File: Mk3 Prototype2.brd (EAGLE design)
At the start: 119.6 x 68 mm, 154 parts, among them IC1 TPD3E001DRL, IC2 TPS62082, IC3 STM32F401V, IC4 BQ2409X, IC6 CC3100MOD, IC7 BQ2970, IC8 LSM6DS3, IC9 LIS3MDL, J1 ZX62-AB-5PA(11), J2 ER-TFT024-3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

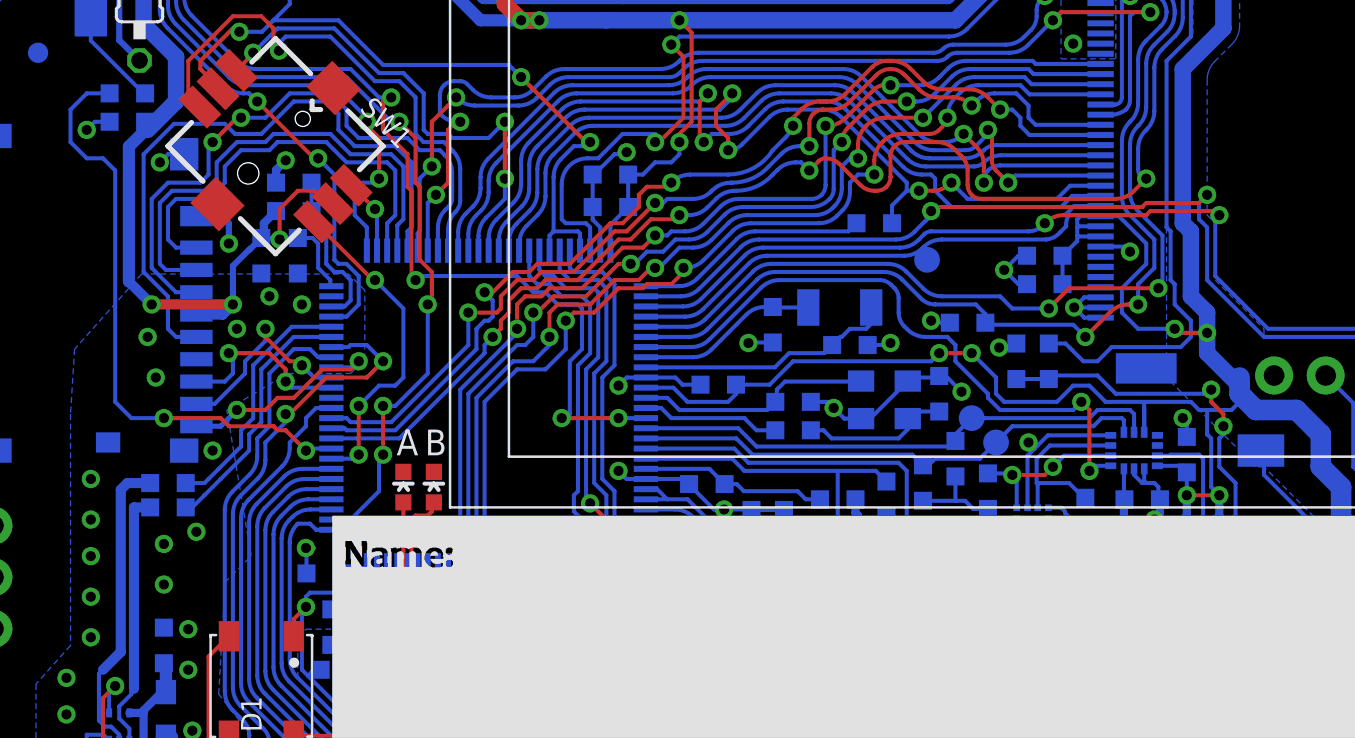
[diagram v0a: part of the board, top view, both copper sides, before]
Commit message: Fix up via clearance
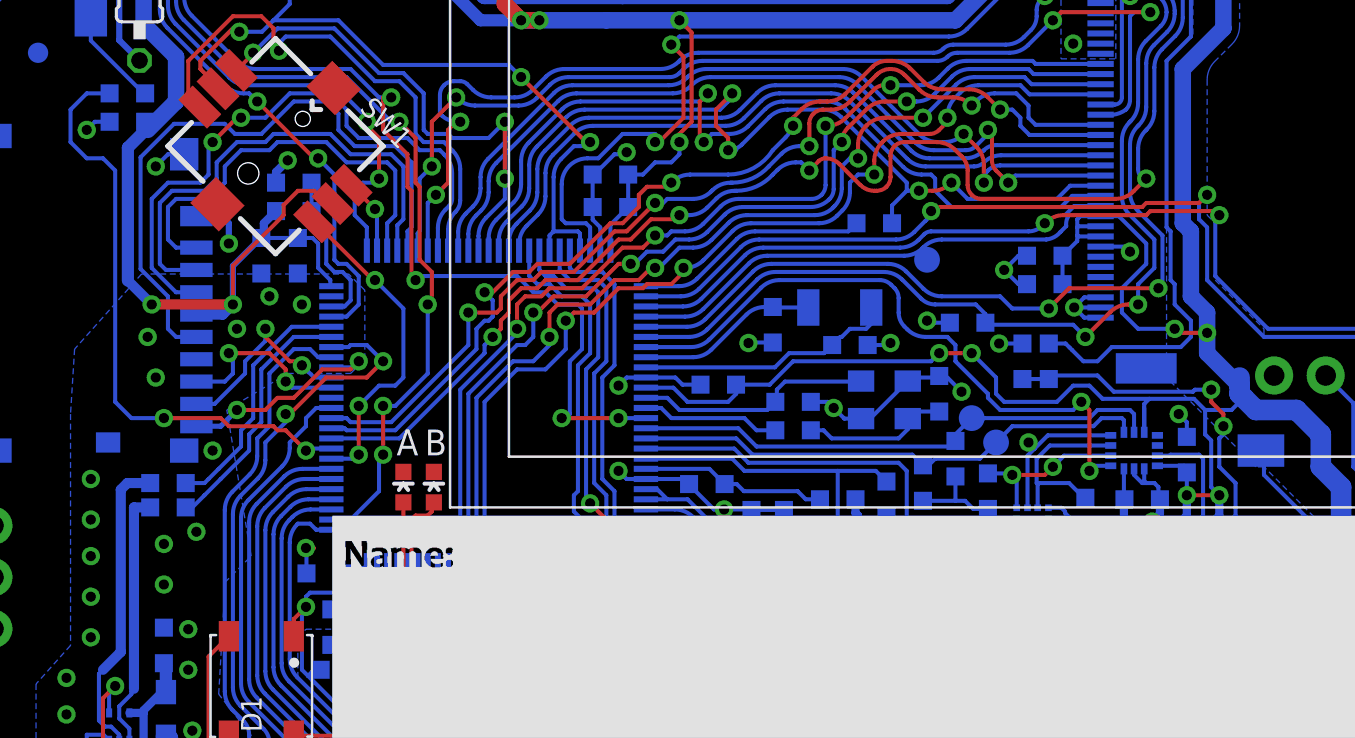
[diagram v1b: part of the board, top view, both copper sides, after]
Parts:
- moved R4 0.30 mm to (58.5, 26.8)
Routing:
- net +3V3: track 526.3 -> 530.2 mm, vias 32 -> 31
- net GND: track 139.9 -> 141.5 mm, vias 155 -> 154

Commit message: minor silk change
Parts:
- moved TP1 2.21 mm to (53.4, 15.8)
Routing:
- net IMU_IRQ1: track 17.0 -> 19.2 mm
- net +3V3: track 530.2 -> 532.3 mm
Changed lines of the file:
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@@
 <element name="LOGO2" library="TiLDA Mk3 Parts" package="UPYTHON_LOGO_SLIKONLY" value="MICROPYTHON-SILK" x="97.2" y="47.9"/>
 <element name="LOGO3" library="TiLDA Mk3 Parts" package="UPYTHON_LOGO_STOPONLY" value="MICROPYTHON-STOP" x="110.9" y="22.9" rot="MR0"/>
-<element name="TP1" library="TiLDA Mk3 Parts" package="B1,27" value="TPB1,27" x="53.6" y="18" smashed="yes" rot="MR0">
-<attribute name="TP_SIGNAL_NAME" value="" x="54.235" y="16.095" size="1" layer="38" rot="MR0"/>
-<attribute name="VALUE" x="54.235" y="17.238" size="0.0254" layer="28" rot="MR0"/>
+<element name="TP1" library="TiLDA Mk3 Parts" package="B1,27" value="TPB1,27" x="53.4" y="15.8" smashed="yes" rot="MR0">
+<attribute name="TP_SIGNAL_NAME" value="" x="54.035" y="13.895" size="1" layer="38" rot="MR0"/>
+<attribute name="VALUE" x="54.035" y="15.038" size="0.0254" layer="28" rot="MR0"/>
 </element>
 </elements>
@@
 <wire x1="56.8" y1="19.525" x2="56.075" y2="19.525" width="0.2" layer="16"/>
 <wire x1="56.8" y1="19.525" x2="56.8" y2="19.2" width="0.2" layer="16"/>
-<wire x1="56.8" y1="19.2" x2="55.2" y2="17.6" width="0.2" layer="16"/>
-<wire x1="55.2" y1="17.6" x2="55.2" y2="16" width="0.2" layer="16"/>
-<wire x1="55.6" y1="15.6" x2="57.125" y2="15.6" width="0.2" layer="16"/>
+<wire x1="55.2" y1="17.6" x2="55.2" y2="15.7" width="0.2" layer="16"/>
+<wire x1="55.2" y1="15.6" x2="57.125" y2="15.6" width="0.2" layer="16"/>
 <wire x1="57.125" y1="15.6" x2="58" y2="16.475" width="0.2" layer="16"/>
 <wire x1="55.675" y1="19.925" x2="56.075" y2="19.525" width="0.2" layer="16"/>
@@
 <wire x1="50.4" y1="19.2" x2="50.4" y2="17.9" width="0.4064" layer="16"/>
 <wire x1="50.4" y1="17.9" x2="50.6" y2="17.7" width="0.4064" layer="16"/>
-<wire x1="50.4" y1="17.9" x2="50.4" y2="16.8" width="0.4064" layer="16"/>
-<wire x1="50.4" y1="16.8" x2="51.2" y2="16" width="0.4064" layer="16"/>
-<wire x1="51.2" y1="16" x2="55.2" y2="16" width="0.4064" layer="16"/>
-<wire x1="55.2" y1="16" x2="55.6" y2="15.6" width="0.4064" layer="16"/>
 <wire x1="62.45" y1="24.95" x2="64.75" y2="24.95" width="0.2" layer="16"/>
 <wire x1="64.75" y1="24.95" x2="66.95" y2="24.95" width="0.2" layer="16"/>
@@
 <wire x1="21.125" y1="33.6" x2="21.725" y2="34.2" width="0.4064" layer="16"/>
 <wire x1="21" y1="32.875" x2="20.975" y2="32.875" width="0.3048" layer="16"/>
+<wire x1="56.8" y1="19.2" x2="55.2" y2="17.6" width="0.2" layer="16"/>
+<wire x1="50.4" y1="17.9" x2="50.4" y2="15.5" width="0.4064" layer="16"/>
+<wire x1="50.4" y1="15.5" x2="51.4" y2="14.5" width="0.4064" layer="16"/>
+<wire x1="51.4" y1="14.5" x2="53.8" y2="14.5" width="0.4064" layer="16"/>
+<wire x1="53.8" y1="14.5" x2="55" y2="15.7" width="0.4064" layer="16"/>
+<wire x1="55" y1="15.7" x2="55.2" y2="15.7" width="0.4064" layer="16"/>
+<wire x1="55.2" y1="15.6" x2="55.2" y2="15.7" width="0.2" layer="16"/>
 </signal>
 <signal name="PB11">
@@
 <wire x1="52.4" y1="21.8" x2="52.8" y2="21.4" width="0.2" layer="16"/>
 <wire x1="52.8" y1="21.4" x2="52.8" y2="19" width="0.2" layer="16"/>
-<wire x1="53.2" y1="18.6" x2="52.8" y2="19" width="0.2" layer="16"/>
+<wire x1="53.4" y1="18.4" x2="52.8" y2="19" width="0.2" layer="16"/>
 <contactref element="TP1" pad="TP"/>
-<wire x1="53.2" y1="18.6" x2="53.2" y2="18.4" width="0.2" layer="16"/>
-<wire x1="53.2" y1="18.4" x2="53.6" y2="18" width="0.2" layer="16"/>
+<wire x1="53.4" y1="15.8" x2="53.4" y2="18.4" width="0.2" layer="16"/>
 </signal>
 <signal name="ADC_IN">

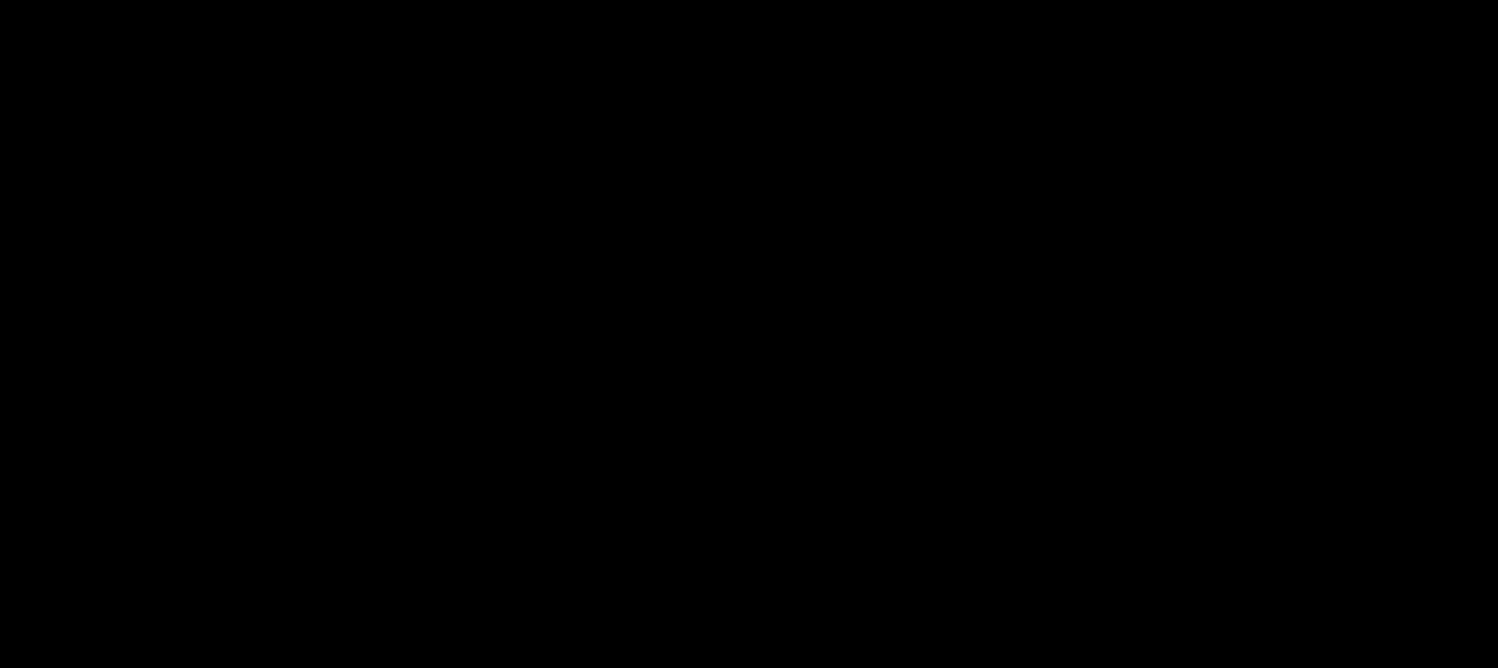
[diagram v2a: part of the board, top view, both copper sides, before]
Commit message: marking HSE crystal as DNP
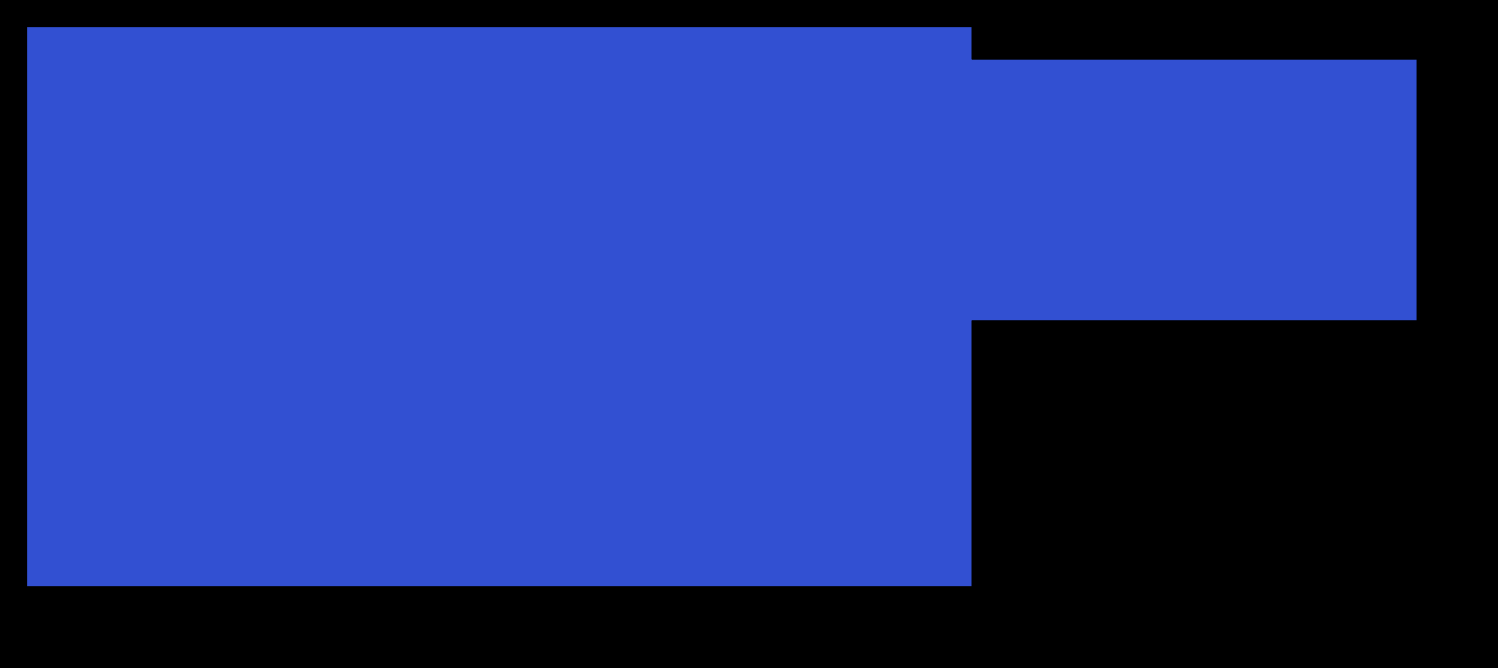
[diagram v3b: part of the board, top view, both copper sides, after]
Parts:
- C20, C21: value 0603/10p/50V/NP0 -> DNP (0603/10p/50V/NP0)
- R43: value 0603/150/5% -> DNP (0603/150/5%)
- X2: value 16MHz-3.2-2.5 -> DNP (16MHz-3.2-2.5)
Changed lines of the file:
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@@
 <layer number="19" name="Unrouted" color="6" fill="1" visible="yes" active="yes"/>
 <layer number="20" name="Dimension" color="15" fill="1" visible="yes" active="yes"/>
-<layer number="21" name="tPlace" color="6" fill="1" visible="no" active="yes"/>
+<layer number="21" name="tPlace" color="6" fill="1" visible="yes" active="yes"/>
 <layer number="22" name="bPlace" color="3" fill="1" visible="yes" active="yes"/>
 <layer number="23" name="tOrigins" color="15" fill="1" visible="yes" active="yes"/>
@@
 <text x="110.4" y="2.8" size="1.016" layer="22" ratio="14" rot="MR0">MFB</text>
 <rectangle x1="64" y1="13.2" x2="82.8" y2="18.8" layer="21"/>
+<rectangle x1="64.8" y1="65.6" x2="98.8" y2="115.6" layer="22" rot="R270"/>
+<rectangle x1="34" y1="94" x2="102" y2="113.2" layer="16"/>
+<rectangle x1="-0.4" y1="74.4" x2="69.2" y2="115.6" layer="16" rot="R180"/>
 </plain>
 <attributes>
@@
 <attribute name="NAME" x="18" y="21.2" size="1.016" layer="26" font="vector" ratio="14" rot="MR180"/>
 </element>
-<element name="X2" library="TiLDA Mk3 Parts" package="CRYSTAL-3.2-2.5" value="16MHz-3.2-2.5" x="51.7" y="24.9" smashed="yes" rot="MR0">
+<element name="X2" library="TiLDA Mk3 Parts" package="CRYSTAL-3.2-2.5" value="DNP (16MHz-3.2-2.5)" x="51.7" y="24.9" smashed="yes" rot="MR0">
 <attribute name="NAME" x="50.65" y="23.2" size="1.016" layer="26" font="vector" ratio="14" rot="MR180"/>
 <attribute name="FARNELL" value="2467444" x="51.7" y="24.9" size="1.778" layer="28" rot="MR0" display="off"/>
 </element>
-<element name="C21" library="TiLDA Mk3 Parts" package="C0603K-SMALL" value="0603/10p/50V/NP0" x="47.2" y="24.8" smashed="yes" rot="MR0">
+<element name="C21" library="TiLDA Mk3 Parts" package="C0603K-SMALL" value="DNP (0603/10p/50V/NP0)" x="47.2" y="24.8" smashed="yes" rot="MR0">
 <attribute name="NAME" x="45.861" y="26.5515" size="1.016" layer="26" font="vector" ratio="14" rot="MR180"/>
 </element>
-<element name="C20" library="TiLDA Mk3 Parts" package="C0603K-SMALL" value="0603/10p/50V/NP0" x="54.4" y="25.2" smashed="yes" rot="MR270">
+<element name="C20" library="TiLDA Mk3 Parts" package="C0603K-SMALL" value="DNP (0603/10p/50V/NP0)" x="54.4" y="25.2" smashed="yes" rot="MR270">
 <attribute name="NAME" x="54.811" y="26.6015" size="1.016" layer="26" font="vector" ratio="14" rot="MR180"/>
 </element>
@@
 <attribute name="NAME" x="12.7" y="47.6" size="1.016" layer="25" font="vector" ratio="14" rot="R270"/>
 </element>
-<element name="R43" library="TiLDA Mk3 Parts" package="C0603K-SMALL" value="0603/150/5%" x="47.2" y="23.4" smashed="yes" rot="MR180">
+<element name="R43" library="TiLDA Mk3 Parts" package="C0603K-SMALL" value="DNP (0603/150/5%)" x="47.2" y="23.4" smashed="yes" rot="MR180">
 <attribute name="NAME" x="48.589" y="21.7985" size="1.016" layer="26" font="vector" ratio="14" rot="MR0"/>
 </element>

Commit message: bom mostly complete (just order numbers for generic passives missing)
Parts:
- D1: value (none) -> WS2812B
- IC4: value BQ2409X -> BQ24092
- R10: value 0603/2k/5% -> 0603/0R
- R13: value 0603/??/5% -> 0603/10k/5%
- R24: value 330/dnp -> 0603/330/5%
- R33: value 0603/100K/5% -> 0603/47k/5%
- R6: value 0603/??/5% -> 0603/2k/5%
- R9: value 0603/??/5% -> 0603/1k/5%
